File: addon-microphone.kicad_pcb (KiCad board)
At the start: 2 copper layers, 61.5 x 26 mm, 3 parts, among them J1 Conn_02x18_Odd_Even, J2 Conn_01x06, J3 Conn_01x06

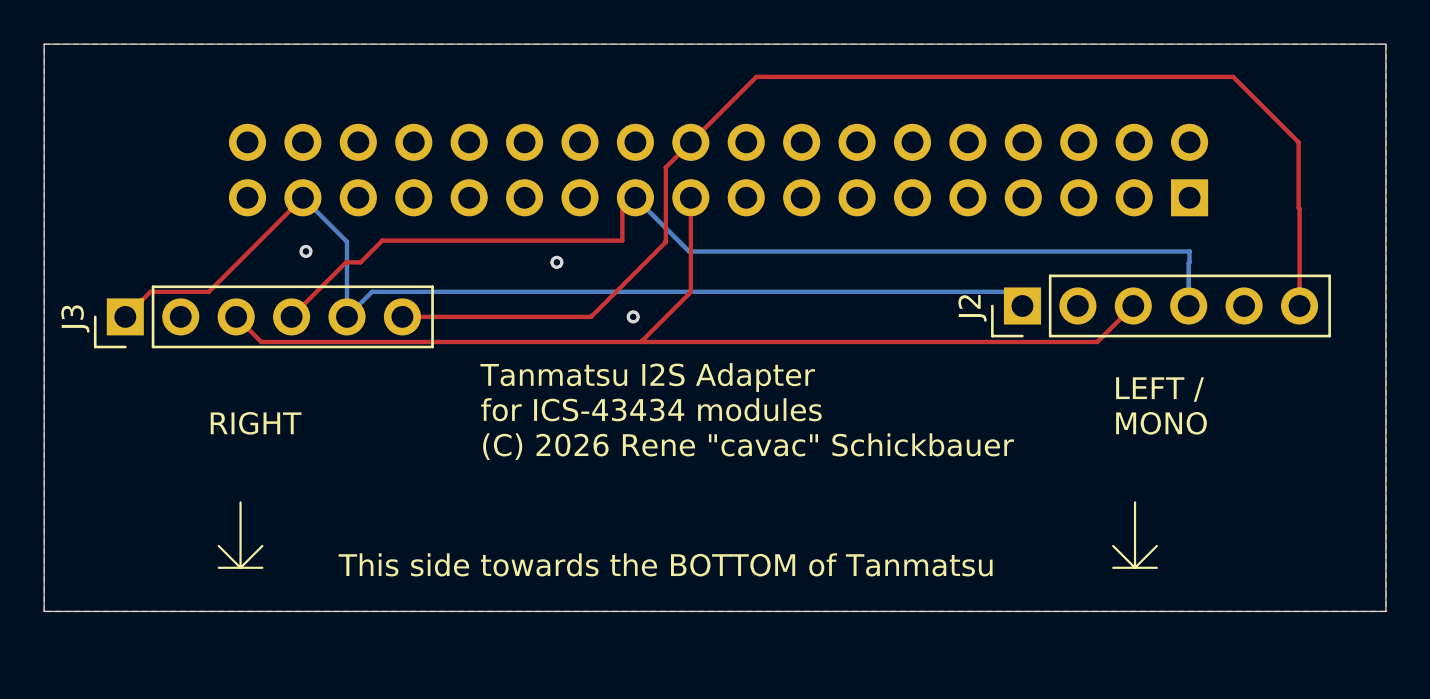
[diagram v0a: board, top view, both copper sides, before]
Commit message: Add I2C EEPROM
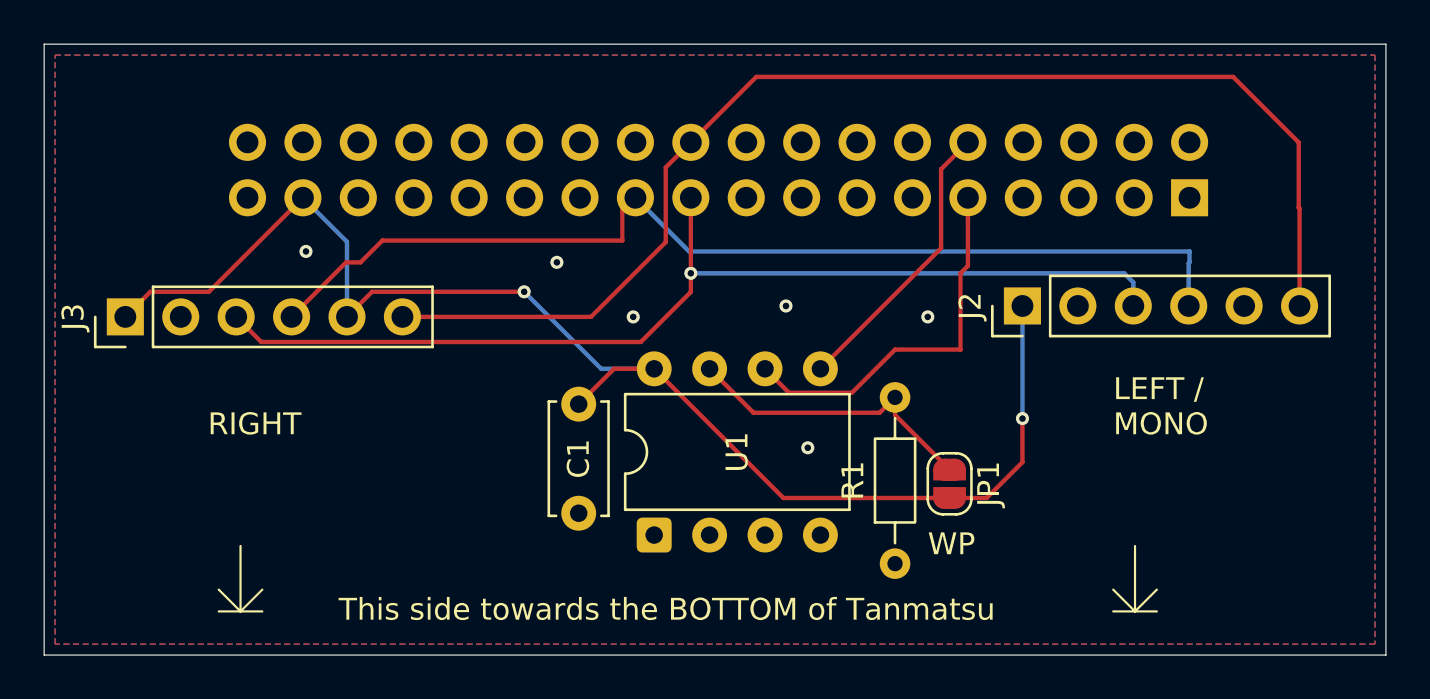
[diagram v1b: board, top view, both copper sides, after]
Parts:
- added C1: 100n, Capacitor_THT:C_Disc_D5.0mm_W2.5mm_P5.00mm, F.Cu at (101.5, 86.5)
- added JP1: Jumper_2_Open, Jumper:SolderJumper-2_P1.3mm_Open_RoundedPad1.0x1.5mm, F.Cu at (118.5, 90.2)
- added R1: 1M, Resistor_THT:R_Axial_DIN0204_L3.6mm_D1.6mm_P7.62mm_Horizontal, F.Cu at (116.0, 93.8)
- added U1: 24C02Cx-x-SN, Package_DIP:DIP-8_W7.62mm, F.Cu at (105.0, 92.5)
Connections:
- J1 pad 10: unconnected-(J1-Pin_10-Pad10) -> I2C_SDA
- J1 pad 9: unconnected-(J1-Pin_9-Pad9) -> I2C_SCK
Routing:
- net I2C_SCK: track 0.00 -> 17.3 mm
- net +3.3V: track 48.4 -> 64.9 mm, vias 0 -> 2
- net Net-(JP1-A): track 0.00 -> 14.0 mm
- net I2C_SDA: track 0.00 -> 13.2 mm
- net SCK: track 49.8 -> 48.1 mm, vias 0 -> 1
- net GND: vias 3 -> 6
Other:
- board size 61.5 x 26 mm -> 61.5 x 28 mm
- board text added: "Tanmatsu I2S Adapter for ICS-43434 modules (C) 2026 Rene Schickbauer"
- board text added: "WP"
- board text removed: "Tanmatsu I2S Adapter for ICS-43434 modules (C) 2026 Rene {dblquote}cavac{dblquote} Schickbauer"
